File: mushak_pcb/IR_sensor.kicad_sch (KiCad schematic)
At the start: 32 parts

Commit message: Add footprints
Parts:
- A1, A2, A3, A4: footprint XDCR_SFH_3015_FA -> SFH_3015_FA:XDCR_SFH_3015_FA
- D2, D3, D4, D5: footprint LED_SFH_4045N -> SFH_4045N:LED_SFH_4045N
- R10, R11, R12, R13, R6, R7, R8, R9: footprint (none) -> Resistor_SMD:R_0805_2012Metric
- TP27, TP31, TP34, TP35, TP38, TP39, TP42: footprint (none) -> TestPoint:TestPoint_Keystone_5019_Minature
- TP28, TP32, TP33, TP36, TP37, TP40, TP41: footprint (none) -> TestPoint:TestPoint_Pad_2.5x2.5mm
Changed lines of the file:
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@@
       (effects (font (size 1.27 1.27)) (justify left))
     )
-    (property "Footprint" "" (id 2) (at 137.922 86.106 0)
+    (property "Footprint" "TestPoint:TestPoint_Keystone_5019_Minature" (id 2) (at 137.922 86.106 0)
       (effects (font (size 1.27 1.27)) hide)
     )
@@
       (effects (font (size 1.27 1.27)) (justify left))
     )
-    (property "Footprint" "XDCR_SFH_3015_FA" (id 2) (at 56.896 97.028 0)
+    (property "Footprint" "SFH_3015_FA:XDCR_SFH_3015_FA" (id 2) (at 56.896 97.028 0)
       (effects (font (size 1.27 1.27)) (justify left bottom) hide)
     )
@@
       (effects (font (size 1.27 1.27)) (justify left))
     )
-    (property "Footprint" "" (id 2) (at 230.124 117.348 0)
+    (property "Footprint" "TestPoint:TestPoint_Pad_2.5x2.5mm" (id 2) (at 230.124 117.348 0)
       (effects (font (size 1.27 1.27)) hide)
     )
@@
       (effects (font (size 1.27 1.27)) (justify left))
     )
-    (property "Footprint" "XDCR_SFH_3015_FA" (id 2) (at 168.402 97.282 0)
+    (property "Footprint" "SFH_3015_FA:XDCR_SFH_3015_FA" (id 2) (at 168.402 97.282 0)
       (effects (font (size 1.27 1.27)) (justify left bottom) hide)
     )
@@
       (effects (font (size 1.27 1.27)) (justify left))
     )
-    (property "Footprint" "" (id 2) (at 131.064 108.458 90)
+    (property "Footprint" "Resistor_SMD:R_0805_2012Metric" (id 2) (at 131.064 108.458 90)
       (effects (font (size 1.27 1.27)) hide)
     )
@@
       (effects (font (size 1.27 1.27)) (justify left))
     )
-    (property "Footprint" "" (id 2) (at 109.982 109.22 90)
+    (property "Footprint" "Resistor_SMD:R_0805_2012Metric" (id 2) (at 109.982 109.22 90)
       (effects (font (size 1.27 1.27)) hide)
     )
@@
       (effects (font (size 1.27 1.27)) (justify left))
     )
-    (property "Footprint" "" (id 2) (at 250.698 86.36 0)
+    (property "Footprint" "TestPoint:TestPoint_Keystone_5019_Minature" (id 2) (at 250.698 86.36 0)
       (effects (font (size 1.27 1.27)) hide)
     )
@@
       (effects (font (size 1.27 1.27)) (justify left))
     )
-    (property "Footprint" "" (id 2) (at 116.84 86.36 0)
+    (property "Footprint" "TestPoint:TestPoint_Pad_2.5x2.5mm" (id 2) (at 116.84 86.36 0)
       (effects (font (size 1.27 1.27)) hide)
     )
@@
       (effects (font (size 1.27 1.27)) (justify left))
     )
-    (property "Footprint" "XDCR_SFH_3015_FA" (id 2) (at 221.996 97.282 0)
+    (property "Footprint" "SFH_3015_FA:XDCR_SFH_3015_FA" (id 2) (at 221.996 97.282 0)
       (effects (font (size 1.27 1.27)) (justify left bottom) hide)
     )
@@
     (property "Reference" "TP39" (id 0) (at 216.408 101.346 90))
     (property "Value" "REC_4" (id 1) (at 217.424 107.188 90))
-    (property "Footprint" "" (id 2) (at 220.98 99.06 0)
+    (property "Footprint" "TestPoint:TestPoint_Keystone_5019_Minature" (id 2) (at 220.98 99.06 0)
       (effects (font (size 1.27 1.27)) hide)
     )
@@
     (property "Reference" "TP35" (id 0) (at 162.814 101.346 90))
     (property "Value" "REC_3" (id 1) (at 163.83 107.188 90))
-    (property "Footprint" "" (id 2) (at 167.386 99.06 0)
+    (property "Footprint" "TestPoint:TestPoint_Keystone_5019_Minature" (id 2) (at 167.386 99.06 0)
       (effects (font (size 1.27 1.27)) hide)
     )
@@
       (effects (font (size 1.27 1.27)) (justify left))
     )
-    (property "Footprint" "LED_SFH_4045N" (id 2) (at 132.842 95.758 0)
+    (property "Footprint" "SFH_4045N:LED_SFH_4045N" (id 2) (at 132.842 95.758 0)
       (effects (font (size 1.27 1.27)) (justify left bottom) hide)
     )
@@
       (effects (font (size 1.27 1.27)) (justify left))
     )
-    (property "Footprint" "LED_SFH_4045N" (id 2) (at 80.518 95.758 0)
+    (property "Footprint" "SFH_4045N:LED_SFH_4045N" (id 2) (at 80.518 95.758 0)
       (effects (font (size 1.27 1.27)) (justify left bottom) hide)
     )
@@
       (effects (font (size 1.27 1.27)) (justify left))
     )
-    (property "Footprint" "" (id 2) (at 197.104 86.36 0)
+    (property "Footprint" "TestPoint:TestPoint_Keystone_5019_Minature" (id 2) (at 197.104 86.36 0)
       (effects (font (size 1.27 1.27)) hide)
     )
@@
       (effects (font (size 1.27 1.27)) (justify left))
     )
-    (property "Footprint" "LED_SFH_4045N" (id 2) (at 245.618 96.012 0)
+    (property "Footprint" "SFH_4045N:LED_SFH_4045N" (id 2) (at 245.618 96.012 0)
       (effects (font (size 1.27 1.27)) (justify left bottom) hide)
     )
@@
       (effects (font (size 1.27 1.27)) (justify left))
     )
-    (property "Footprint" "" (id 2) (at 176.022 86.614 0)
+    (property "Footprint" "TestPoint:TestPoint_Pad_2.5x2.5mm" (id 2) (at 176.022 86.614 0)
       (effects (font (size 1.27 1.27)) hide)
     )
@@
       (effects (font (size 1.27 1.27)) (justify left))
     )
-    (property "Footprint" "" (id 2) (at 57.658 109.22 90)
+    (property "Footprint" "Resistor_SMD:R_0805_2012Metric" (id 2) (at 57.658 109.22 90)
       (effects (font (size 1.27 1.27)) hide)
     )
@@
       (effects (font (size 1.27 1.27)) (justify left))
     )
-    (property "Footprint" "" (id 2) (at 229.616 86.614 0)
+    (property "Footprint" "TestPoint:TestPoint_Pad_2.5x2.5mm" (id 2) (at 229.616 86.614 0)
       (effects (font (size 1.27 1.27)) hide)
     )
@@
       (effects (font (size 1.27 1.27)) (justify left))
     )
-    (property "Footprint" "XDCR_SFH_3015_FA" (id 2) (at 109.22 97.028 0)
+    (property "Footprint" "SFH_3015_FA:XDCR_SFH_3015_FA" (id 2) (at 109.22 97.028 0)
       (effects (font (size 1.27 1.27)) (justify left bottom) hide)
     )
@@
       (effects (font (size 1.27 1.27)) (justify left))
     )
-    (property "Footprint" "LED_SFH_4045N" (id 2) (at 192.024 96.012 0)
+    (property "Footprint" "SFH_4045N:LED_SFH_4045N" (id 2) (at 192.024 96.012 0)
       (effects (font (size 1.27 1.27)) (justify left bottom) hide)
     )
@@
       (effects (font (size 1.27 1.27)) (justify left))
     )
-    (property "Footprint" "" (id 2) (at 190.246 108.712 90)
+    (property "Footprint" "Resistor_SMD:R_0805_2012Metric" (id 2) (at 190.246 108.712 90)
       (effects (font (size 1.27 1.27)) hide)
     )
@@
     (property "Reference" "TP31" (id 0) (at 103.632 101.092 90))
     (property "Value" "REC_2" (id 1) (at 104.648 106.934 90))
-    (property "Footprint" "" (id 2) (at 108.204 98.806 0)
+    (property "Footprint" "TestPoint:TestPoint_Keystone_5019_Minature" (id 2) (at 108.204 98.806 0)
       (effects (font (size 1.27 1.27)) hide)
     )
@@
       (effects (font (size 1.27 1.27)) (justify left))
     )
-    (property "Footprint" "" (id 2) (at 64.516 86.36 0)
+    (property "Footprint" "TestPoint:TestPoint_Pad_2.5x2.5mm" (id 2) (at 64.516 86.36 0)
       (effects (font (size 1.27 1.27)) hide)
     )
@@
       (effects (font (size 1.27 1.27)) (justify left))
     )
-    (property "Footprint" "" (id 2) (at 243.84 108.712 90)
+    (property "Footprint" "Resistor_SMD:R_0805_2012Metric" (id 2) (at 243.84 108.712 90)
       (effects (font (size 1.27 1.27)) hide)
     )
@@
     (property "Reference" "TP27" (id 0) (at 51.308 101.092 90))
     (property "Value" "REC_1" (id 1) (at 52.324 106.934 90))
-    (property "Footprint" "" (id 2) (at 55.88 98.806 0)
+    (property "Footprint" "TestPoint:TestPoint_Keystone_5019_Minature" (id 2) (at 55.88 98.806 0)
       (effects (font (size 1.27 1.27)) hide)
     )
@@
       (effects (font (size 1.27 1.27)) (justify left))
     )
-    (property "Footprint" "" (id 2) (at 176.53 117.348 0)
+    (property "Footprint" "TestPoint:TestPoint_Pad_2.5x2.5mm" (id 2) (at 176.53 117.348 0)
       (effects (font (size 1.27 1.27)) hide)
     )
@@
       (effects (font (size 1.27 1.27)) (justify left))
     )
-    (property "Footprint" "" (id 2) (at 222.758 109.474 90)
+    (property "Footprint" "Resistor_SMD:R_0805_2012Metric" (id 2) (at 222.758 109.474 90)
       (effects (font (size 1.27 1.27)) hide)
     )
@@
       (effects (font (size 1.27 1.27)) (justify left))
     )
-    (property "Footprint" "" (id 2) (at 117.348 117.094 0)
+    (property "Footprint" "TestPoint:TestPoint_Pad_2.5x2.5mm" (id 2) (at 117.348 117.094 0)
       (effects (font (size 1.27 1.27)) hide)
     )
@@
       (effects (font (size 1.27 1.27)) (justify left))
     )
-    (property "Footprint" "" (id 2) (at 169.164 109.474 90)
+    (property "Footprint" "Resistor_SMD:R_0805_2012Metric" (id 2) (at 169.164 109.474 90)
       (effects (font (size 1.27 1.27)) hide)
     )
@@
       (effects (font (size 1.27 1.27)) (justify left))
     )
-    (property "Footprint" "" (id 2) (at 78.74 108.458 90)
-      (effects (font (size 1.27 1.27)) hide)
-    )
+    (property "Footprint" "Resistor_SMD:R_0805_2012Metric" (id 2) (at 78.74 108.458 90)
+      (effects (font (size 1.27 1.27)) hide)
+    )

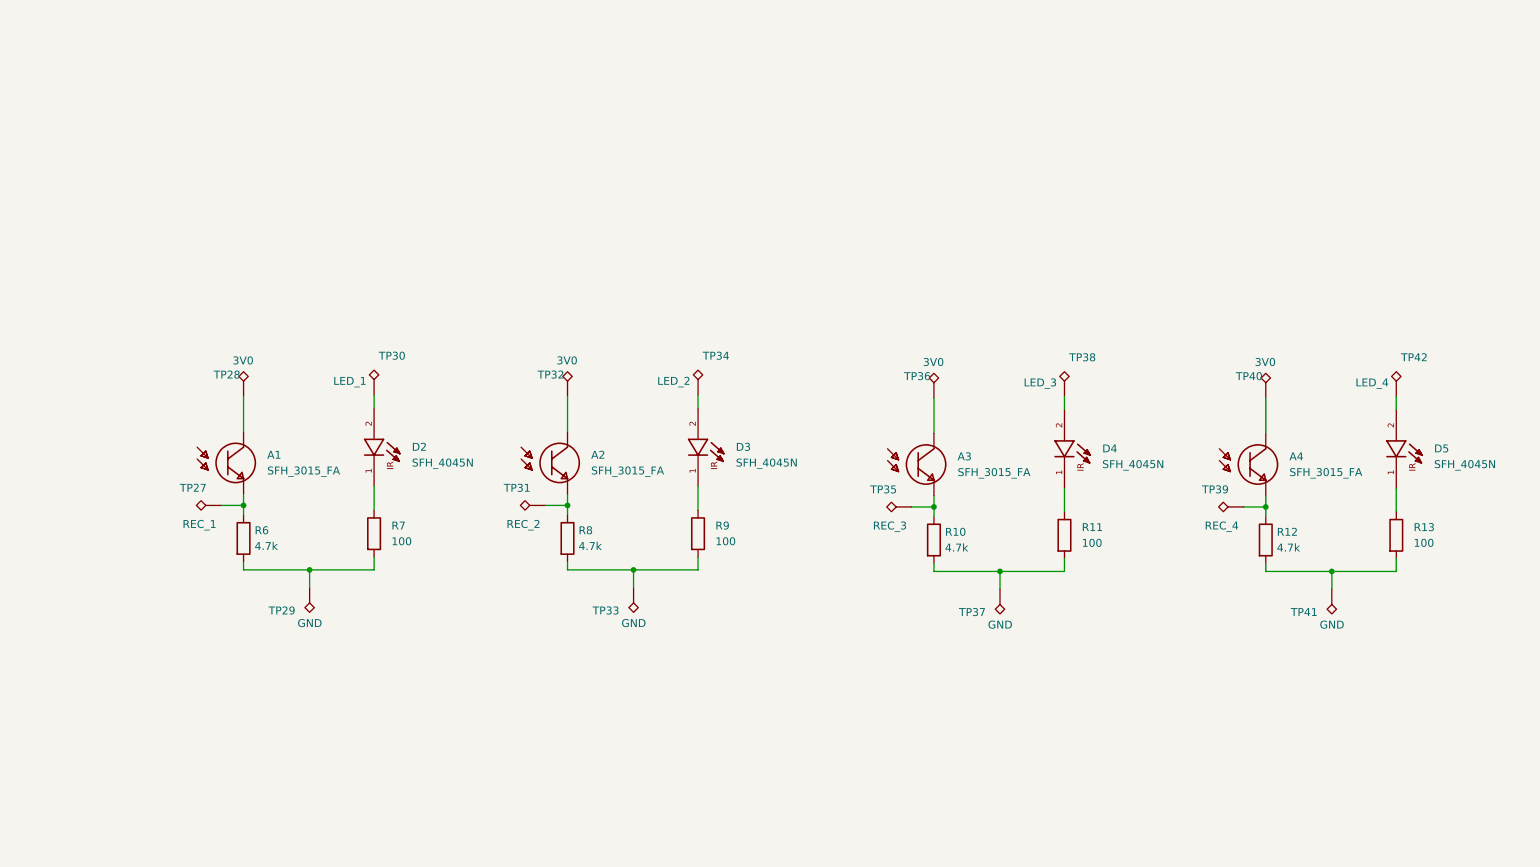
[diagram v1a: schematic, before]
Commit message: Update Schematics and footprints for sensors
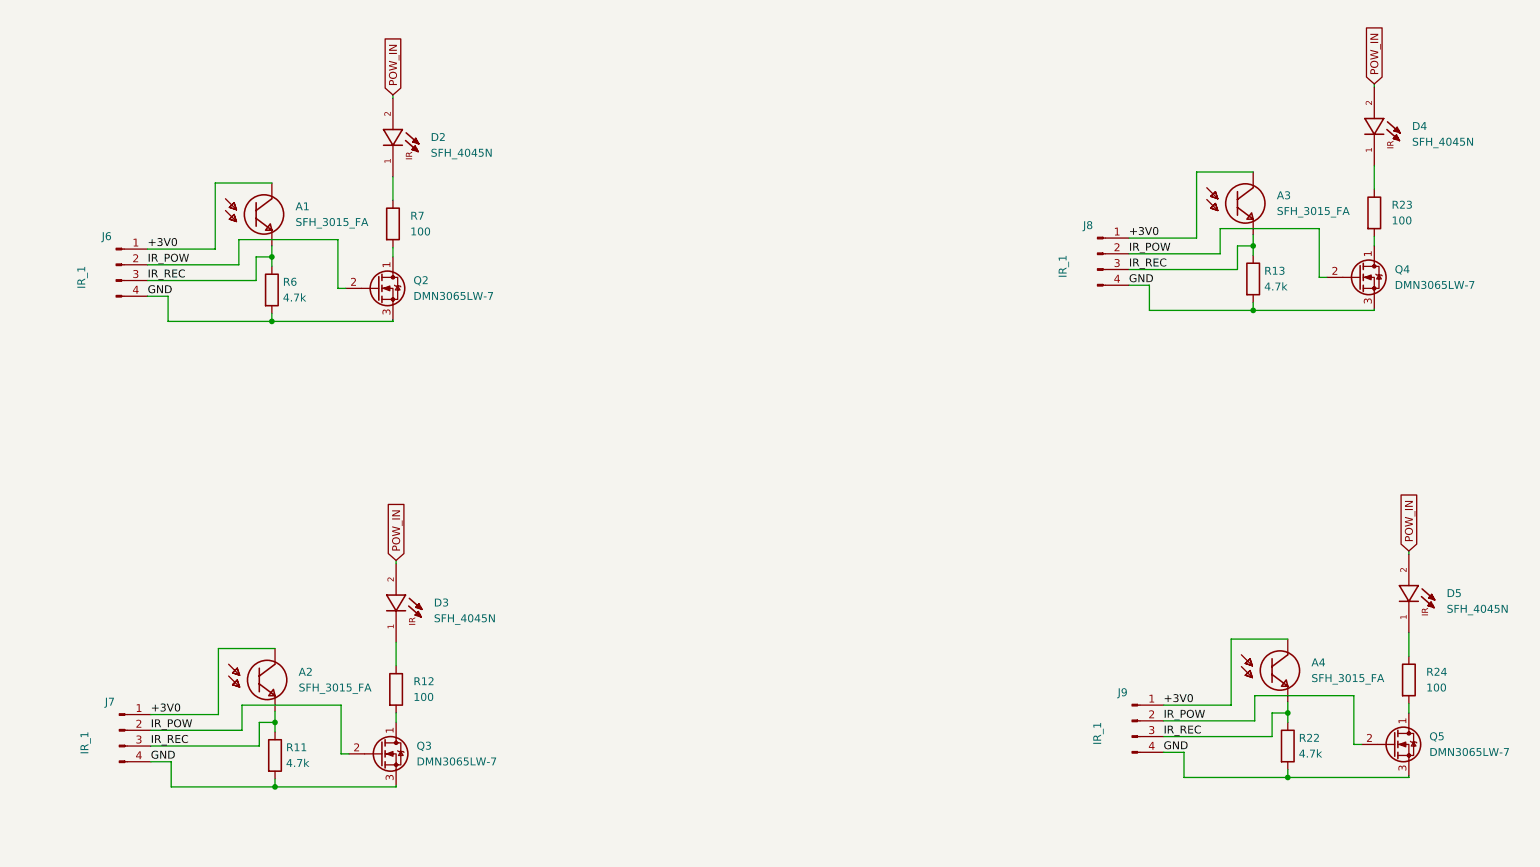
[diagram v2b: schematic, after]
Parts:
- removed R10, R8: 4.7k, Resistor_SMD:R_0805_2012Metric, symbol Device:R
- removed R9: 100, Resistor_SMD:R_0805_2012Metric, symbol Device:R
- removed TP27: REC_1, TestPoint:TestPoint_Keystone_5019_Minature, symbol Connector:TestPoint_Alt
- removed TP28, TP32, TP36, TP40: 3V0, TestPoint:TestPoint_Pad_2.5x2.5mm, symbol Connector:TestPoint_Alt
- removed TP29, TP33, TP37, TP41: GND, TestPoint:TestPoint_Pad_2.5x2.5mm, symbol Connector:TestPoint_Alt
- removed TP30: LED_1, TestPoint:TestPoint_Keystone_5019_Minature, symbol Connector:TestPoint_Alt
- removed TP31: REC_2, TestPoint:TestPoint_Keystone_5019_Minature, symbol Connector:TestPoint_Alt
- removed TP34: LED_2, TestPoint:TestPoint_Keystone_5019_Minature, symbol Connector:TestPoint_Alt
- removed TP35: REC_3, TestPoint:TestPoint_Keystone_5019_Minature, symbol Connector:TestPoint_Alt
- removed TP38: LED_3, TestPoint:TestPoint_Keystone_5019_Minature, symbol Connector:TestPoint_Alt
- removed TP39: REC_4, TestPoint:TestPoint_Keystone_5019_Minature, symbol Connector:TestPoint_Alt
- removed TP42: LED_4, TestPoint:TestPoint_Keystone_5019_Minature, symbol Connector:TestPoint_Alt
- added J6, J7, J8, J9: IR_1, mushak_mount_footprint:IR_SLAVE_V_04, symbol Connector:Conn_01x04_Male
- added Q2, Q3, Q4, Q5: DMN3065LW-7, Package_TO_SOT_SMD:SOT-323_SC-70, symbol Device:Q_NMOS_DGS
- added R22: 4.7k, Resistor_SMD:R_0402_1005Metric, symbol Device:R
- added R23, R24: 100, Resistor_SMD:R_0402_1005Metric, symbol Device:R
- R11, R13: value 100 -> 4.7k; footprint Resistor_SMD:R_0805_2012Metric -> Resistor_SMD:R_0402_1005Metric
- R12: value 4.7k -> 100; footprint Resistor_SMD:R_0805_2012Metric -> Resistor_SMD:R_0402_1005Metric
- R6, R7: footprint Resistor_SMD:R_0805_2012Metric -> Resistor_SMD:R_0402_1005Metric
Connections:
- net at R7.2: now also Q2.1 (D); no longer R6.2
- net POW_IN: now reaches D3.2
- net POW_IN: now also D2.2, D4.2, D5.2
- net IR_REC: now reaches A1.1, R6.1
- net IR_REC: now also A2.1, A3.1, A4.1, R11.1, R13.1, J6.3 (Pin_3), J7.3 (Pin_3), J8.3 (Pin_3), J9.3 (Pin_3), R22.1
- net +3V0: now reaches A1.2
- net +3V0: now also A2.2, A3.2, A4.2, J6.1 (Pin_1), J7.1 (Pin_1), J8.1 (Pin_1), J9.1 (Pin_1)
- net at R12.2: now also Q3.1 (D); no longer R13.2
- net at D3.1: now also R12.1
- net at D5.1: now also R24.1; no longer R13.1
- net at D4.1: now also R23.1; no longer R11.1
- net GND: now reaches R11.2
- net GND: now also R13.2, R6.2, J6.4 (Pin_4), J7.4 (Pin_4), J8.4 (Pin_4), J9.4 (Pin_4), Q2.3 (S), Q3.3 (S), Q4.3 (S), Q5.3 (S), R22.2
- new net: Q4.1 (D), R23.2
- new net: Q5.1 (D), R24.2
- new net IR_POW: J6.2 (Pin_2), J7.2 (Pin_2), J8.2 (Pin_2), J9.2 (Pin_2), Q2.2 (G), Q3.2 (G), Q4.2 (G), Q5.2 (G)
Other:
- moved on the sheet: A1, D2, R6, R7

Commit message: changed footprints of capacitors and resistors
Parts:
- R11, R13, R22, R6: footprint Resistor_SMD:R_0402_1005Metric -> Resistor_SMD:R_0201_0603Metric
- R12, R23, R24, R7: footprint Resistor_SMD:R_0402_1005Metric -> Resistor_SMD:R_0603_1608Metric
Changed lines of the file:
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@@
       (effects (font (size 1.27 1.27)) (justify left))
     )
-    (property "Footprint" "Resistor_SMD:R_0402_1005Metric" (id 2) (at 62.738 144.272 90)
+    (property "Footprint" "Resistor_SMD:R_0201_0603Metric" (id 2) (at 62.738 144.272 90)
       (effects (font (size 1.27 1.27)) hide)
     )
@@
       (effects (font (size 1.27 1.27)) (justify left))
     )
-    (property "Footprint" "Resistor_SMD:R_0402_1005Metric" (id 2) (at 226.314 142.748 90)
+    (property "Footprint" "Resistor_SMD:R_0201_0603Metric" (id 2) (at 226.314 142.748 90)
       (effects (font (size 1.27 1.27)) hide)
     )
@@
       (effects (font (size 1.27 1.27)) (justify left))
     )
-    (property "Footprint" "Resistor_SMD:R_0402_1005Metric" (id 2) (at 62.23 69.088 90)
+    (property "Footprint" "Resistor_SMD:R_0201_0603Metric" (id 2) (at 62.23 69.088 90)
       (effects (font (size 1.27 1.27)) hide)
     )
@@
       (effects (font (size 1.27 1.27)) (justify left))
     )
-    (property "Footprint" "Resistor_SMD:R_0402_1005Metric" (id 2) (at 220.726 67.31 90)
+    (property "Footprint" "Resistor_SMD:R_0201_0603Metric" (id 2) (at 220.726 67.31 90)
       (effects (font (size 1.27 1.27)) hide)
     )
@@
       (effects (font (size 1.27 1.27)) (justify left))
     )
-    (property "Footprint" "Resistor_SMD:R_0402_1005Metric" (id 2) (at 240.284 56.642 90)
+    (property "Footprint" "Resistor_SMD:R_0603_1608Metric" (id 2) (at 240.284 56.642 90)
       (effects (font (size 1.27 1.27)) hide)
     )
@@
       (effects (font (size 1.27 1.27)) (justify left))
     )
-    (property "Footprint" "Resistor_SMD:R_0402_1005Metric" (id 2) (at 245.872 132.08 90)
+    (property "Footprint" "Resistor_SMD:R_0603_1608Metric" (id 2) (at 245.872 132.08 90)
       (effects (font (size 1.27 1.27)) hide)
     )
@@
       (effects (font (size 1.27 1.27)) (justify left))
     )
-    (property "Footprint" "Resistor_SMD:R_0402_1005Metric" (id 2) (at 82.296 133.604 90)
+    (property "Footprint" "Resistor_SMD:R_0603_1608Metric" (id 2) (at 82.296 133.604 90)
       (effects (font (size 1.27 1.27)) hide)
     )
@@
       (effects (font (size 1.27 1.27)) (justify left))
     )
-    (property "Footprint" "Resistor_SMD:R_0402_1005Metric" (id 2) (at 81.788 58.42 90)
-      (effects (font (size 1.27 1.27)) hide)
-    )
+    (property "Footprint" "Resistor_SMD:R_0603_1608Metric" (id 2) (at 81.788 58.42 90)
+      (effects (font (size 1.27 1.27)) hide)
+    )
